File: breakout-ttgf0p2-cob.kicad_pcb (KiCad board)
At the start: 4 copper layers, 50 x 50 mm, 106 parts, among them J1 Conn_01x12, J2 DF12NB-60DS-0.5V_51, J3 DF12NB-50DS-0.5V_51, U1 AP2112K-3.3, U2 AP2112K-3.3, U3 TT_GF_0p2_ASIC, U4 24LC02

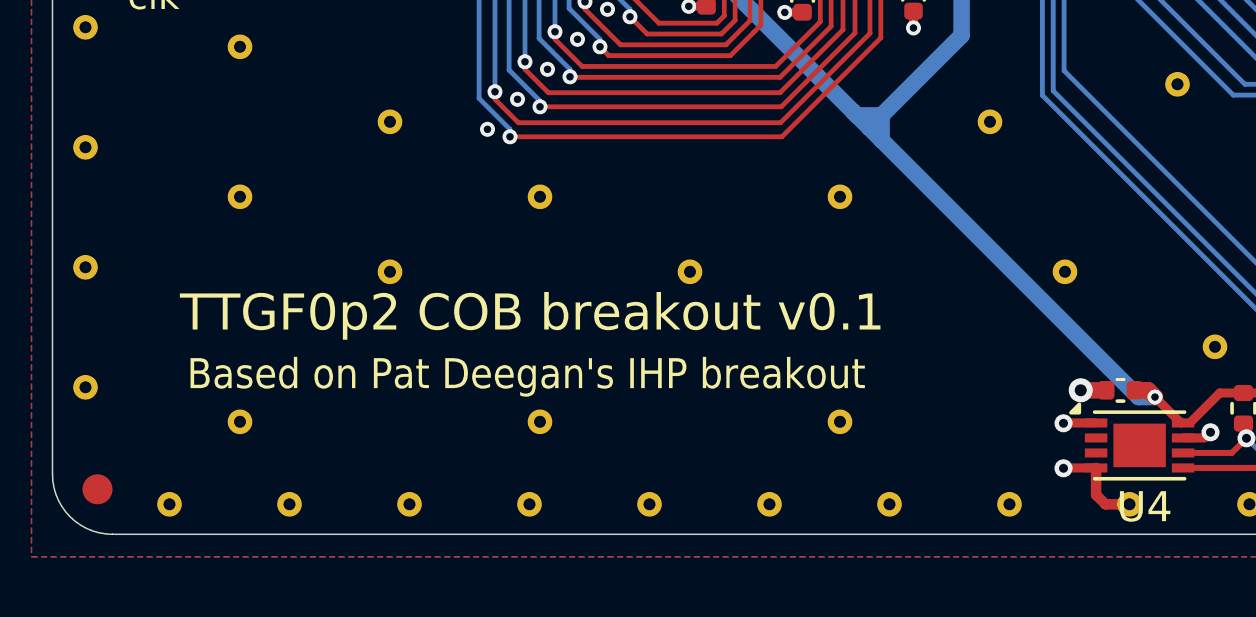
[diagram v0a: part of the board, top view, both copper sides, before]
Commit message: add silkscreen for marking TTP2 vs TTPG
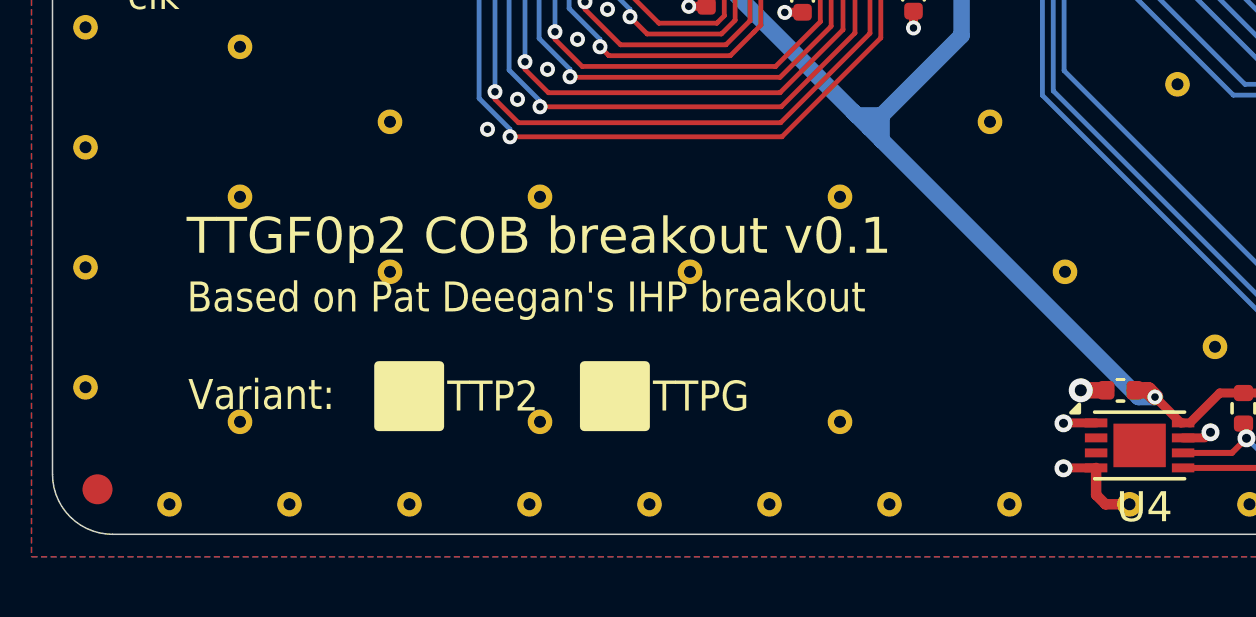
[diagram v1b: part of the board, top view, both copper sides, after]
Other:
- board text added: "TTP2"
- board text added: "TTPG"
- board text added: "Variant:"
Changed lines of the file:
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@@
+		(layer "F.SilkS")
+	)
+	(gr_rect
+		(start 130.7308 93.37825)
+		(end 132.7628 95.41025)
+		(stroke
+			(width 0.3)
+			(type solid)
+		)
+		(fill yes)
 		(layer "F.SilkS")
 	)
@@
 			(type default)
 		)
+		(layer "F.SilkS")
+	)
+	(gr_rect
+		(start 123.8728 93.37825)
+		(end 125.9048 95.41025)
+		(stroke
+			(width 0.3)
+			(type solid)
+		)
+		(fill yes)
 		(layer "F.SilkS")
 	)
@@
 	)
 	(gr_text "Based on Pat Deegan's IHP breakout"
-		(at 117.48 94.25 0)
+		(at 117.48 91.694 0)
 		(layer "F.SilkS")
 		(effects
@@
 		)
 	)
+	(gr_text "TTPG"
+		(at 133.0168 94.996 0)
+		(layer "F.SilkS")
+		(effects
+			(font
+				(size 1 0.9)
+				(thickness 0.15)
+			)
+			(justify left bottom)
+		)
+	)
 	(gr_text "*"
 		(at 139.1 52.95 0)
@@
 	)
 	(gr_text "TTGF0p2 COB breakout v${REVISION}"
-		(at 117.25 92.32 0)
+		(at 117.472 89.7636 0)
 		(layer "F.SilkS")
 		(effects
@@
 		)
 	)
+	(gr_text "TTP2"
+		(at 126.1588 94.996 0)
+		(layer "F.SilkS")
+		(effects
+			(font
+				(size 1 0.9)
+				(thickness 0.15)
+			)
+			(justify left bottom)
+		)
+	)
+	(gr_text "Variant:"
+		(at 117.5228 94.9452 0)
+		(layer "F.SilkS")
+		(effects
+			(font
+				(size 1 0.9)
+				(thickness 0.15)
+			)
+			(justify left bottom)
+		)
+	)
